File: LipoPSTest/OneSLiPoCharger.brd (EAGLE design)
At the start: 86.4 x 52.1 mm, 58 parts, among them IC1 LM358N, Q1 BUZ10

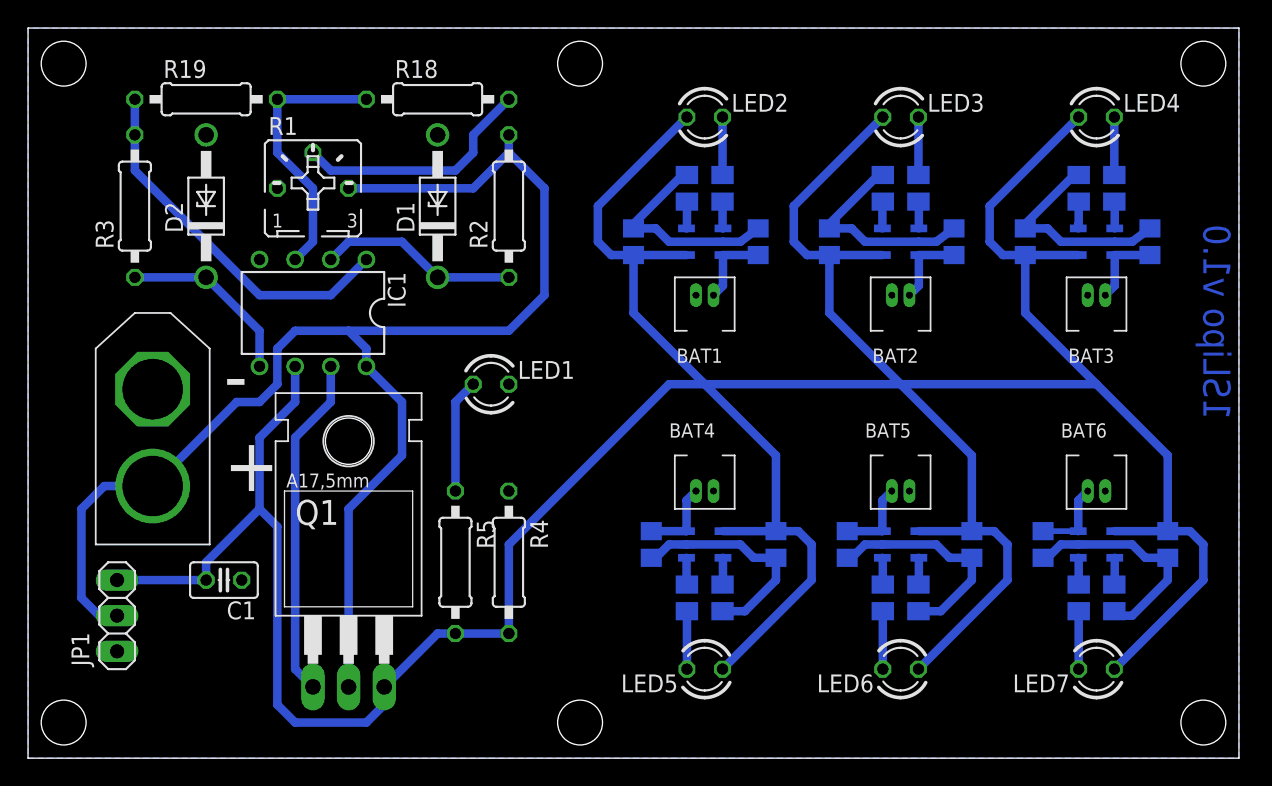
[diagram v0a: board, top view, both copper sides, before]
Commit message: Add lipo charger test circuits
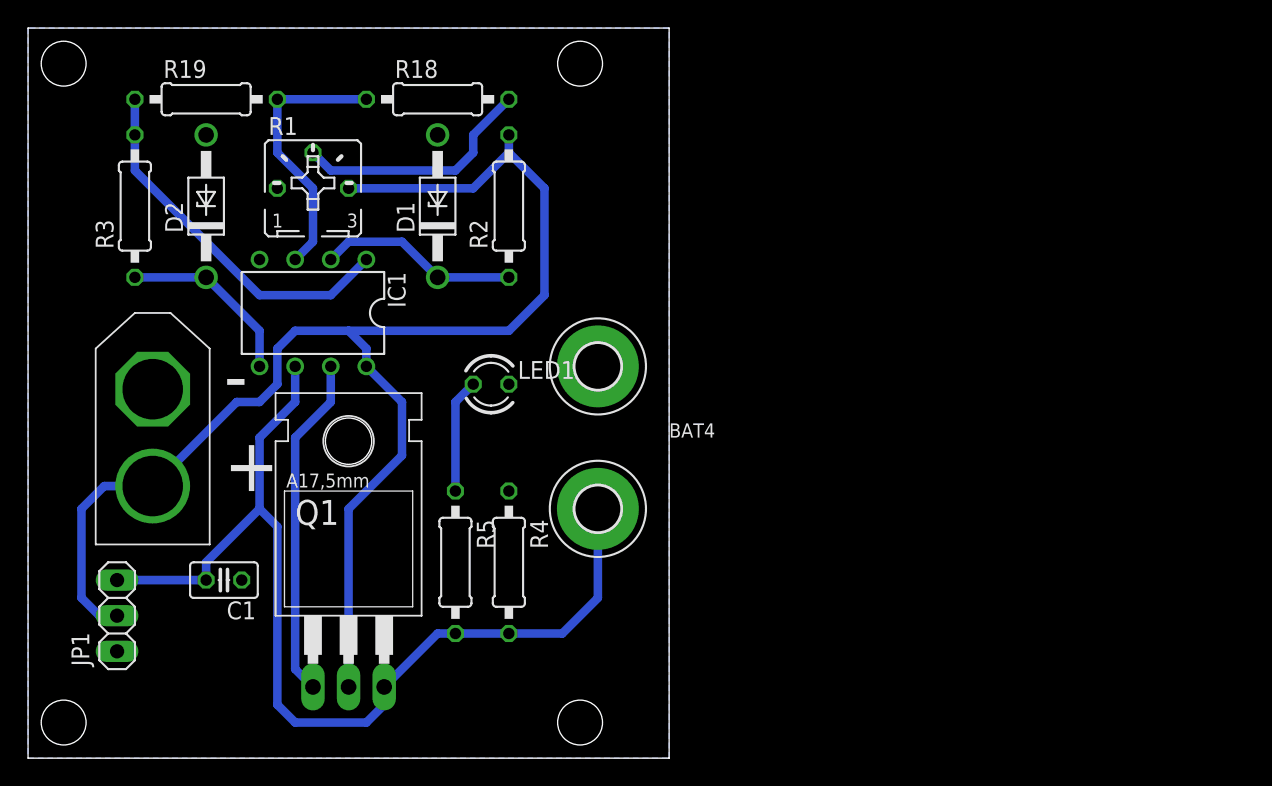
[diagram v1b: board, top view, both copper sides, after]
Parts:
- removed C10, C11, C12, C13, C2, C3, C4, C5, C6, C7, C8, C9: 4.7uF, rcl:C0805
- removed LED2, LED3, LED4, LED5, LED6, LED7: (no value), led:LED3MM
- removed R10, R12, R14, R16, R6, R8: (no value), rcl:M0805
- removed R11, R13, R15, R17, R7, R9: 3.9k, rcl:M0805
- removed U$1, U$10, U$12, U$4, U$6, U$8: MCP73831, MCP73831:MCP73831-SOT23
- removed U$11, U$13, U$2, U$5, U$7, U$9: PICOBLADE-2PIN, Picoblade:PICOBLADE-2PIN
- added H1, H2: MOUNT-PAD-ROUND3.3, holes:3,3-PAD
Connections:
- removed net N$11: LED3.K, R8.2
- removed net N$12: R8.1, U$4.1
- removed net N$13: R9.2, U$4.5
- removed net N$14: C5.2, U$4.3, U$5.P$2
- removed net N$15: LED4.K, R10.2
- removed net N$16: R10.1, U$6.1
- removed net N$17: R11.2, U$6.5
- removed net N$18: C7.2, U$6.3, U$7.P$2
- removed net N$19: LED5.K, R12.2
- removed net N$20: R12.1, U$8.1
- removed net N$21: R13.2, U$8.5
- removed net N$22: C9.2, U$8.3, U$9.P$2
- removed net N$23: LED6.K, R14.2
- removed net N$24: R14.1, U$10.1
- removed net N$25: R15.2, U$10.5
- removed net N$26: C11.2, U$10.3, U$11.P$2
- removed net N$27: LED7.K, R16.2
- removed net N$28: R16.1, U$12.1
- removed net N$29: R17.2, U$12.5
- removed net N$30: C13.2, U$12.3, U$13.P$2
- removed net N$6: LED2.K, R6.2
- removed net N$7: R6.1, U$1.1
- removed net N$8: R7.2, U$1.5
- removed net N$9: C3.2, U$1.3, U$2.P$2
- net +5V: now also H1.B3,3; no longer C10.1, C12.1, C2.1, C4.1, C6.1, C8.1, LED2.A, LED3.A, LED4.A, LED5.A, LED6.A, LED7.A, U$1.4, U$10.4, U$12.4, U$4.4, U$6.4, U$8.4
- net GND: now also H2.B3,3; no longer C10.2, C11.1, C12.2, C13.1, C2.2, C3.1, C4.2, C5.1, C6.2, C7.1, C8.2, C9.1, R11.1, R13.1, R15.1, R17.1, R7.1, R9.1, U$1.2, U$10.2, U$11.P$1, U$12.2, U$13.P$1, U$2.P$1, U$4.2, U$5.P$1, U$6.2, U$7.P$1, U$8.2, U$9.P$1
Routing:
- net +5V: track 293.2 -> 72.9 mm
- net GND: track 94.4 -> 0.00 mm
- net N$14: track 5.97 -> 0.00 mm
- net N$18: track 5.65 -> 0.00 mm
- net N$30: track 5.65 -> 0.00 mm
- net N$9: track 5.65 -> 0.00 mm
- net N$26: track 5.65 -> 0.00 mm
- net N$22: track 5.65 -> 0.00 mm
- net N$27: track 4.13 -> 0.00 mm
- net N$23: track 4.13 -> 0.00 mm
- net N$19: track 4.13 -> 0.00 mm
- net N$6: track 4.13 -> 0.00 mm
- net N$15: track 4.13 -> 0.00 mm
- net N$11: track 4.13 -> 0.00 mm
- net N$21: track 1.94 -> 0.00 mm
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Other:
- board size 86.4 x 52.1 mm -> 45.7 x 52.1 mm
- board text removed: "1SLipo v1.0"
- board text removed: "BAT1"
- board text removed: "BAT2"
- board text removed: "BAT3"
- board text removed: "BAT5"
- board text removed: "BAT6"
